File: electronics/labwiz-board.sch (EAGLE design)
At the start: 97 parts, among them J1 SD_MICRO_SDIO_1BIT, J2 CORTEX_DEBUGSMD, J3 DNP, U1 STM32F10XRXT6, U2 MCP73831/2, U4 MIC5219-3.3V, X2 M12_BOTTOM_CONTACTS_FPC_1MM, Y3 32.768kHz

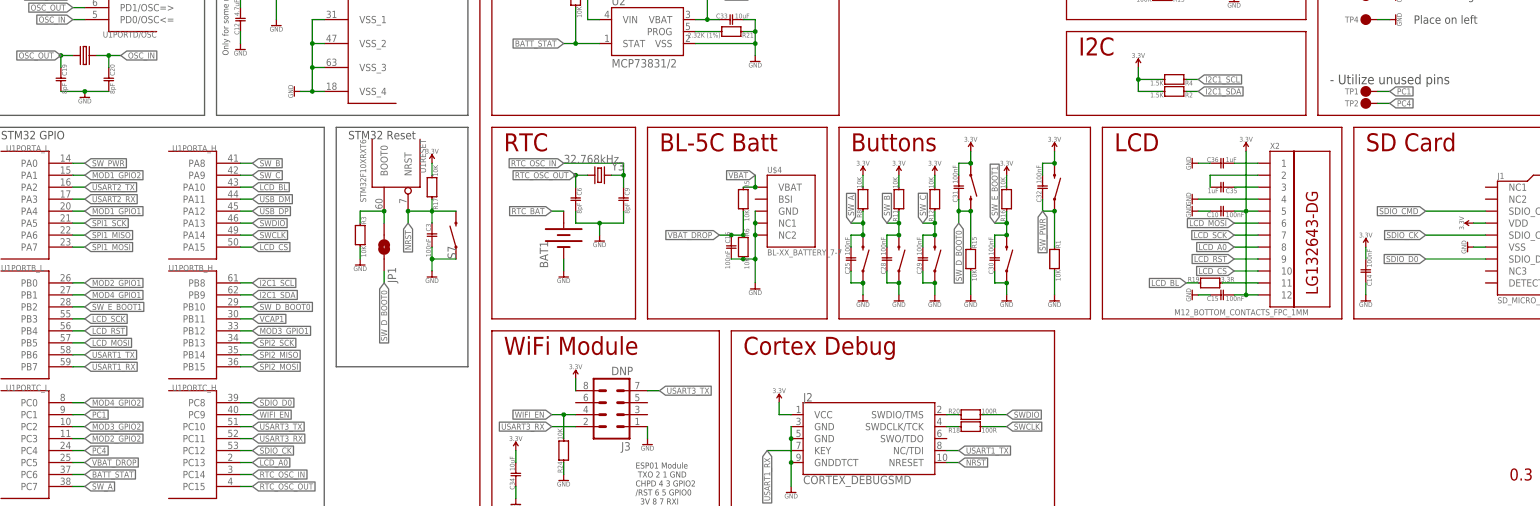
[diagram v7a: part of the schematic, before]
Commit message: Added circuitry to alow PC1 to put BOOT0 into bootloader mode. I also had to switch around SW_E from normally high to normally low.
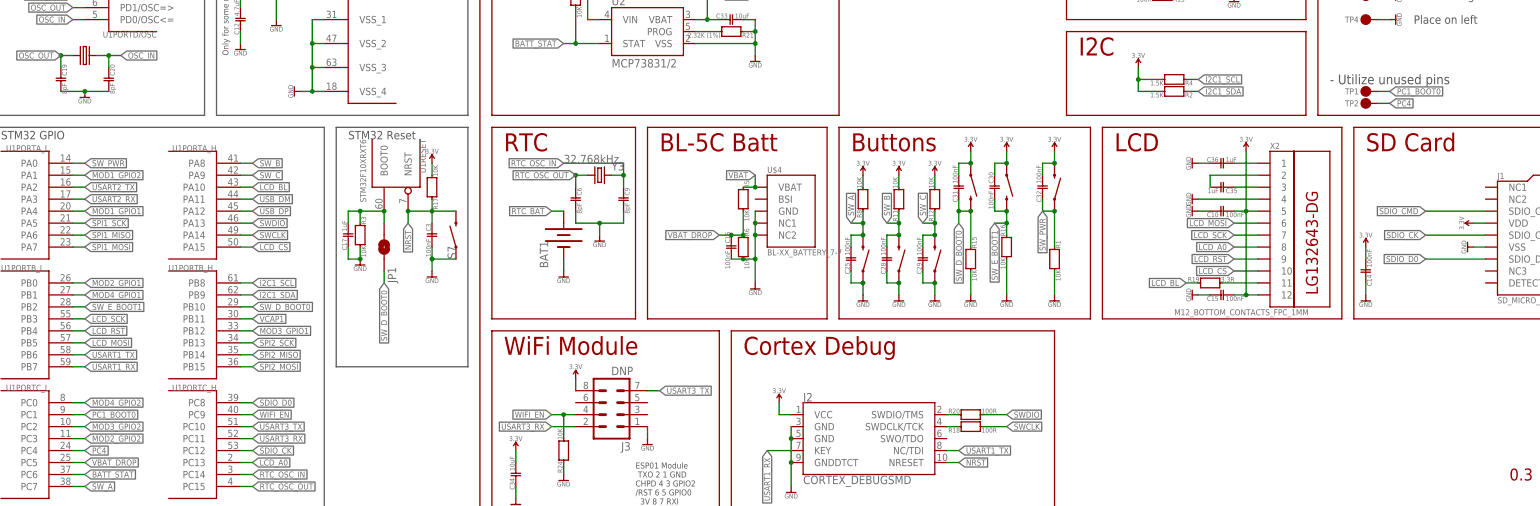
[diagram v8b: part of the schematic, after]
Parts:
- added C17: 1uF, PaxInstruments-RCL:CAPACITOR_FIXED_1UF_0402
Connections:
- removed net BOOT0: JP1.2, R3.2, U1RESET.BOOT0
- removed net PC1: TP1.P$1, U1PORTC_L.PC1
- new net PC1_BOOT0: C17.2, JP1.2, R3.2, TP1.P$1, U1PORTC_L.PC1, U1RESET.BOOT0
- net 3.3V: now also C30.1, S5.1; no longer R16.1
- net GND: now also C17.1, R16.1; no longer C30.1, S5.1
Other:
- moved on the sheet: C30, R16
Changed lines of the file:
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@@
 <part name="R13" library="PaxInstruments-RCL" deviceset="RESISTOR_FIXED" device="_0402" technology="_100K" value="100K"/>
 <part name="SUPPLY5" library="PaxInstruments-Aesthetics" deviceset="SYM_VCC" device="" technology="3.3V" value="3.3V"/>
+<part name="C17" library="PaxInstruments-RCL" deviceset="CAPACITOR_FIXED" device="_0402" technology="_1UF" value="1uF"/>
 </parts>
 <sheets>
@@
 <attribute name="POPULATE" x="215.9" y="60.96" size="1.778" layer="96" rot="R180" display="off"/>
 </instance>
-<instance part="R16" gate="G$1" x="223.52" y="73.66">
-<attribute name="MPN" x="223.52" y="73.66" size="1.778" layer="96" display="off"/>
-<attribute name="POPULATE" x="223.52" y="73.66" size="1.778" layer="96" display="off"/>
+<instance part="R16" gate="G$1" x="223.52" y="63.5" rot="MR180">
+<attribute name="MPN" x="223.52" y="63.5" size="1.778" layer="96" rot="MR180" display="off"/>
+<attribute name="POPULATE" x="223.52" y="63.5" size="1.778" layer="96" rot="MR180" display="off"/>
 </instance>
 <instance part="C26" gate="G$1" x="134.62" y="170.18">
@@
 <attribute name="MPN" x="215.9" y="76.2" size="1.778" layer="96" rot="R270" display="off"/>
 </instance>
-<instance part="S5" gate="G$1" x="223.52" y="60.96" smashed="yes" rot="MR90">
-<attribute name="MF" x="223.52" y="60.96" size="1.778" layer="96" rot="MR90" display="off"/>
-<attribute name="MPN" x="223.52" y="60.96" size="1.778" layer="96" rot="MR90" display="off"/>
+<instance part="S5" gate="G$1" x="223.52" y="76.2" smashed="yes" rot="R270">
+<attribute name="MF" x="223.52" y="76.2" size="1.778" layer="96" rot="R270" display="off"/>
+<attribute name="MPN" x="223.52" y="76.2" size="1.778" layer="96" rot="R270" display="off"/>
 </instance>
 <instance part="R19" gate="G$1" x="266.7" y="55.88" rot="R270">
@@
 </instance>
 <instance part="P+6" gate="G$1" x="233.68" y="83.82" rot="MR0"/>
-<instance part="P+7" gate="G$1" x="223.52" y="78.74" rot="MR0"/>
+<instance part="P+7" gate="G$1" x="223.52" y="83.82" rot="MR0"/>
 <instance part="P+8" gate="G$1" x="215.9" y="83.82" rot="MR0"/>
 <instance part="P+10" gate="G$1" x="193.04" y="78.74" rot="MR0"/>
@@
 <instance part="C28" gate="G$1" x="198.12" y="60.96"/>
 <instance part="C29" gate="G$1" x="205.74" y="60.96"/>
-<instance part="C30" gate="G$1" x="220.98" y="60.96"/>
+<instance part="C30" gate="G$1" x="220.98" y="76.2" rot="MR180"/>
 <instance part="C31" gate="G$1" x="213.36" y="76.2"/>
 <instance part="C32" gate="G$1" x="231.14" y="76.2"/>
@@
 <instance part="R13" gate="G$1" x="256.54" y="116.84" rot="R90"/>
 <instance part="SUPPLY5" gate="G$1" x="243.84" y="121.92"/>
+<instance part="C17" gate="G$1" x="83.82" y="66.04"/>
 </instances>
 <busses>
@@
 <wire x1="231.14" y1="81.28" x2="231.14" y2="78.74" width="0.1524" layer="91"/>
 <junction x="233.68" y="81.28"/>
-</segment>
-<segment>
-<pinref part="P+7" gate="G$1" pin="3.3V"/>
-<pinref part="R16" gate="G$1" pin="1"/>
-<wire x1="223.52" y1="76.2" x2="223.52" y2="78.74" width="0.1524" layer="91"/>
 </segment>
 <segment>
@@
 <junction x="243.84" y="119.38"/>
 </segment>
+<segment>
+<pinref part="S5" gate="G$1" pin="1"/>
+<pinref part="C30" gate="G$1" pin="1"/>
+<wire x1="223.52" y1="81.28" x2="220.98" y2="81.28" width="0.1524" layer="91"/>
+<wire x1="220.98" y1="81.28" x2="220.98" y2="78.74" width="0.1524" layer="91"/>
+<pinref part="P+7" gate="G$1" pin="3.3V"/>
+<wire x1="223.52" y1="81.28" x2="223.52" y2="83.82" width="0.1524" layer="91"/>
+<junction x="223.52" y="81.28"/>
+</segment>
 </net>
 <net name="GND" class="5">
@@
 <wire x1="198.12" y1="55.88" x2="198.12" y2="58.42" width="0.1524" layer="91"/>
 <junction x="200.66" y="55.88"/>
-</segment>
-<segment>
-<pinref part="S5" gate="G$1" pin="1"/>
-<pinref part="GND33" gate="G$1" pin="GND"/>
-<wire x1="223.52" y1="53.34" x2="223.52" y2="55.88" width="0.1524" layer="91"/>
-<pinref part="C30" gate="G$1" pin="1"/>
-<wire x1="223.52" y1="55.88" x2="220.98" y2="55.88" width="0.1524" layer="91"/>
-<wire x1="220.98" y1="55.88" x2="220.98" y2="58.42" width="0.1524" layer="91"/>
-<junction x="223.52" y="55.88"/>
 </segment>
 <segment>
@@
 <pinref part="GND3" gate="G$1" pin="GND"/>
 <wire x1="86.36" y1="60.96" x2="86.36" y2="63.5" width="0.1524" layer="91"/>
+<pinref part="C17" gate="G$1" pin="1"/>
+<wire x1="83.82" y1="63.5" x2="83.82" y2="60.96" width="0.1524" layer="91"/>
+<wire x1="83.82" y1="60.96" x2="86.36" y2="60.96" width="0.1524" layer="91"/>
+<junction x="86.36" y="60.96"/>
 </segment>
 <segment>
@@
 <wire x1="271.78" y1="119.38" x2="271.78" y2="116.84" width="0.1524" layer="91"/>
 <pinref part="TP10" gate="G$1" pin="P$1"/>
+</segment>
+<segment>
+<pinref part="R16" gate="G$1" pin="1"/>
+<pinref part="GND33" gate="G$1" pin="GND"/>
+<wire x1="223.52" y1="60.96" x2="223.52" y2="53.34" width="0.1524" layer="91"/>
 </segment>
 </net>
@@
 </segment>
 </net>
-<net name="BOOT0" class="0">
+<net name="PC1_BOOT0" class="0">
 <segment>
 <pinref part="U1" gate="RESET" pin="BOOT0"/>
@@
 <junction x="91.44" y="71.12"/>
 <pinref part="JP1" gate="G$1" pin="2"/>
+<pinref part="C17" gate="G$1" pin="2"/>
+<wire x1="83.82" y1="68.58" x2="83.82" y2="71.12" width="0.1524" layer="91"/>
+<wire x1="83.82" y1="71.12" x2="86.36" y2="71.12" width="0.1524" layer="91"/>
+<junction x="86.36" y="71.12"/>
+</segment>
+<segment>
+<pinref part="U1" gate="PORTC_L" pin="PC1"/>
+<wire x1="25.4" y1="27.94" x2="27.94" y2="27.94" width="0.1524" layer="91"/>
+<label x="27.94" y="27.94" size="1.27" layer="95" xref="yes"/>
+</segment>
+<segment>
+<wire x1="302.26" y1="96.52" x2="304.8" y2="96.52" width="0.1524" layer="91"/>
+<label x="304.8" y="96.52" size="1.27" layer="95" xref="yes"/>
+<pinref part="TP1" gate="G$1" pin="P$1"/>
 </segment>
 </net>
@@
 <pinref part="R16" gate="G$1" pin="2"/>
 <pinref part="S5" gate="G$1" pin="2"/>
-<wire x1="223.52" y1="66.04" x2="223.52" y2="68.58" width="0.1524" layer="91"/>
-<wire x1="223.52" y1="68.58" x2="223.52" y2="71.12" width="0.1524" layer="91"/>
-<label x="220.98" y="68.58" size="1.27" layer="95" rot="R90" xref="yes"/>
+<wire x1="223.52" y1="71.12" x2="223.52" y2="68.58" width="0.1524" layer="91"/>
+<wire x1="223.52" y1="68.58" x2="223.52" y2="66.04" width="0.1524" layer="91"/>
+<label x="220.98" y="68.58" size="1.27" layer="95" rot="MR270" xref="yes"/>
 <wire x1="220.98" y1="68.58" x2="223.52" y2="68.58" width="0.1524" layer="91"/>
 <junction x="223.52" y="68.58"/>
 <pinref part="C30" gate="G$1" pin="2"/>
-<wire x1="223.52" y1="66.04" x2="220.98" y2="66.04" width="0.1524" layer="91"/>
-<wire x1="220.98" y1="66.04" x2="220.98" y2="63.5" width="0.1524" layer="91"/>
-<junction x="223.52" y="66.04"/>
+<wire x1="223.52" y1="71.12" x2="220.98" y2="71.12" width="0.1524" layer="91"/>
+<wire x1="220.98" y1="71.12" x2="220.98" y2="73.66" width="0.1524" layer="91"/>
+<junction x="223.52" y="71.12"/>
 </segment>
 </net>
@@
 </segment>
 </net>
-<net name="PC1" class="0">
-<segment>
-<pinref part="U1" gate="PORTC_L" pin="PC1"/>
-<wire x1="25.4" y1="27.94" x2="27.94" y2="27.94" width="0.1524" layer="91"/>
-<label x="27.94" y="27.94" size="1.27" layer="95" xref="yes"/>
-</segment>
-<segment>
-<wire x1="302.26" y1="96.52" x2="304.8" y2="96.52" width="0.1524" layer="91"/>
-<label x="304.8" y="96.52" size="1.27" layer="95" xref="yes"/>
-<pinref part="TP1" gate="G$1" pin="P$1"/>
-</segment>
-</net>
